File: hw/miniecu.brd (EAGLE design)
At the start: 50 x 50 mm, 59 parts

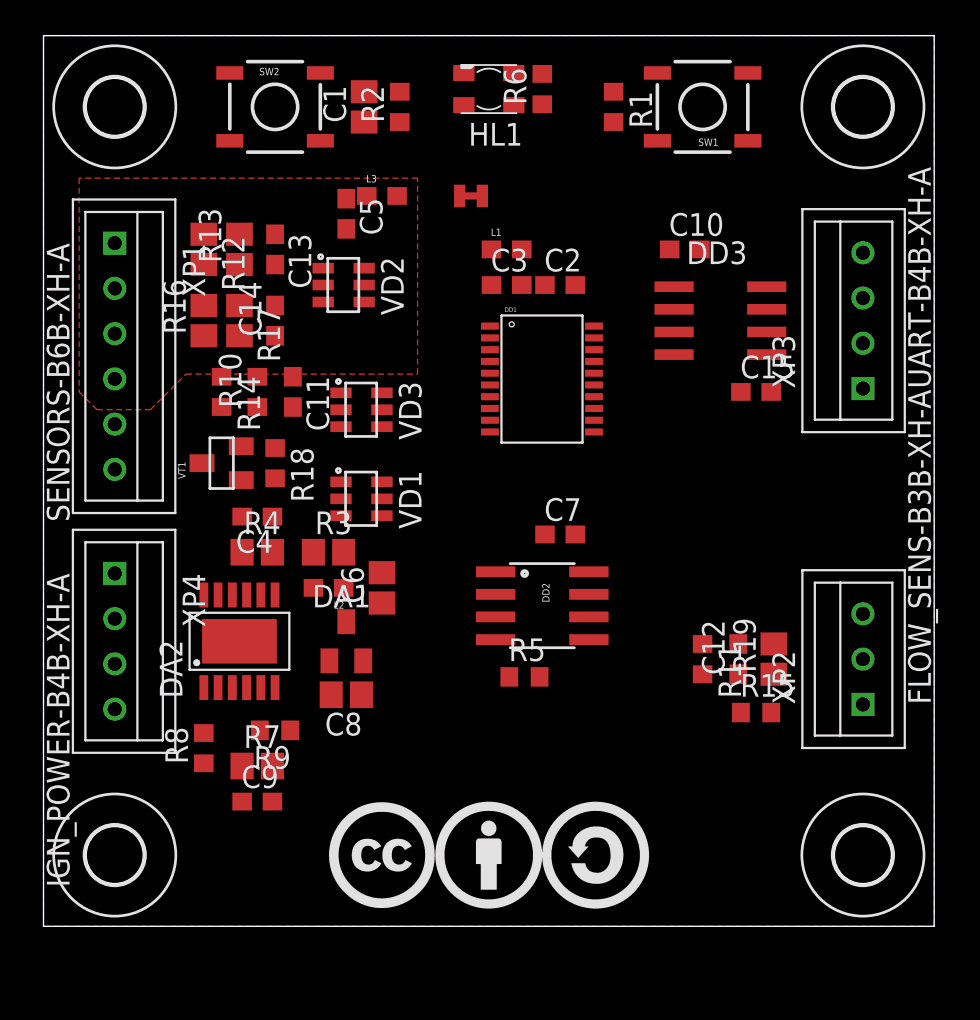
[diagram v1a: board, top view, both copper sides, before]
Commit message: use two resistors in voltage divider
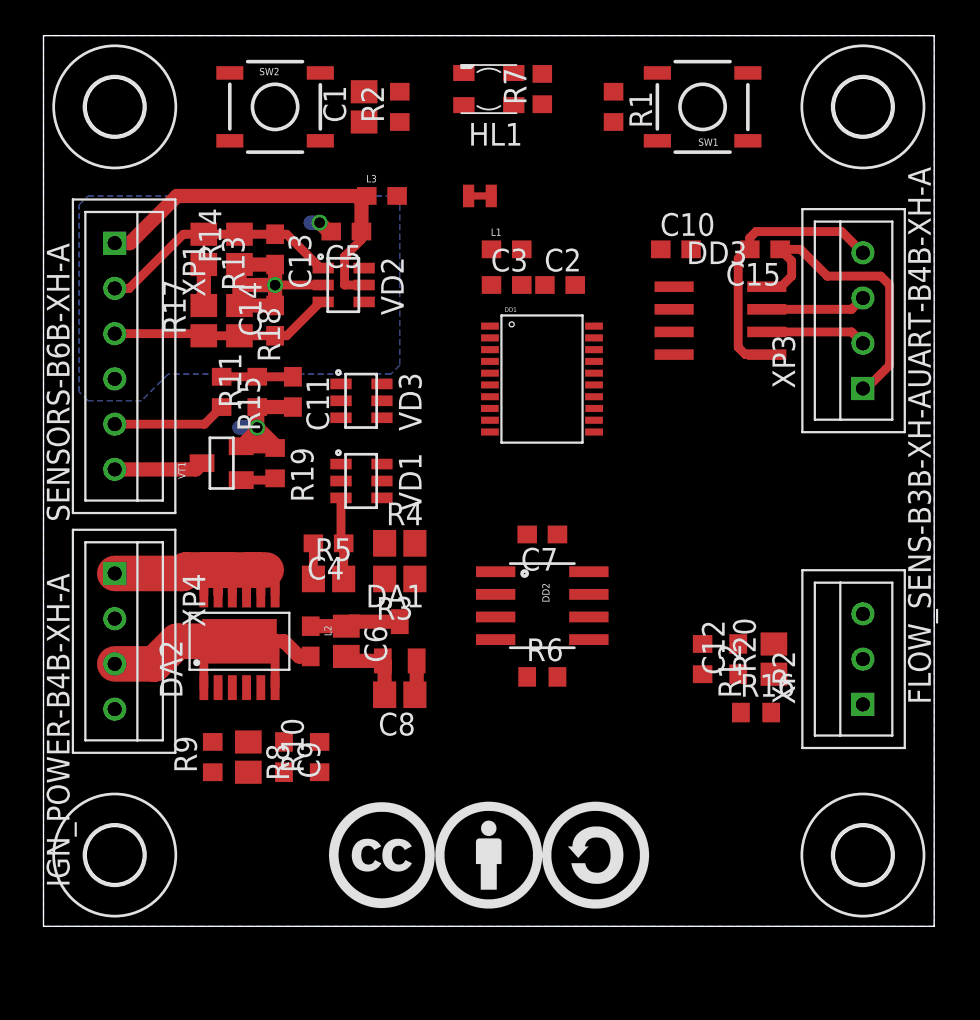
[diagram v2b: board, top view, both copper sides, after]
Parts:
- added R20: 10k, resistor:R0805
- R10, R13, R17: value np -> 10k
- R12: value 10k -> np; device resistor:R0805 -> resistor:R0603
- R14: value 100 -> np; device resistor:R0603 -> resistor:R0805
- R16: value 10k -> 100; device resistor:R0805 -> resistor:R0603
- R18: value 5.1k -> np; device resistor:R0603 -> resistor:R0805
- R19: value 10k -> 5.1k; device resistor:R0805 -> resistor:R0603
- R5: device resistor:R0603 -> resistor:R0805
- R6: value 140 -> 10k
- R7: value 10k -> 140; device resistor:R0805 -> resistor:R0603
- R8: value 100 -> 10k; device resistor:R0603 -> resistor:R0805
- R9: value 10k -> 100
- moved H1 42.0 mm to (46.0, 4.00)
- moved H2 42.0 mm to (4.00, 4.00)
- moved R7 41.2 mm to (28.0, 47.0), turned to 90 degrees
- moved R16 38.0 mm to (40.0, 12.0), turned to 0 degrees
- moved R12 36.2 mm to (37.0, 15.0)
- moved R15 35.0 mm to (10.0, 30.0), turned to 270 degrees
- moved R6 33.0 mm to (28.0, 14.0), turned to 0 degrees
- moved R19 30.1 mm to (13.0, 26.0), turned to 270 degrees
- moved R11 29.2 mm to (12.0, 30.0), turned to 90 degrees
- moved R10 20.8 mm to (15.5, 9.50)
- moved R5 12.3 mm to (16.0, 19.5)
- moved R18 8.25 mm to (11.0, 34.0)
- moved R14 8.06 mm to (11.0, 38.0), turned to 90 degrees
- moved C15 8.02 mm to (40.5, 38.0), turned to 180 degrees
- moved R4 8.02 mm to (20.0, 21.5)
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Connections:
- new net N$1: R3.1, R4.2
- net +3V3: now also R20.2, R6.2; no longer R19.2, R5.2
- net AGND: now also R14.1, R18.1; no longer R13.1, R17.1
- net AVCC_EXT: now also R13.2, R17.2; no longer R12.2, R16.2
- net FLOW_PULSE: now also R12.2, R16.1; no longer R11.2, R15.1
- net GND: now also R12.1, R19.1, R5.1, R8.2; no longer R18.1, R4.1, R7.2, R9.1
- net IGN_EN: now also R9.1; no longer R8.1
- net I_SENSE: now also R8.1; no longer R7.1
- net LED: now also R7.1; no longer R6.1
- net N$2: now also R7.2; no longer R6.2
- net N$3: now also R6.1; no longer R5.1
- net N$4: now also R16.2, R20.1; no longer R15.2, R19.1
- net N$7: now also R9.2; no longer R8.2
- net N$9: now also R10.2; no longer R9.2
- net OIL_PRES: now also R17.1, R18.2; no longer R16.1, R17.2
- net RPM_IN: now also R11.2, R15.1; no longer R10.2, R14.1
- net RPM_IN_CON: now also R15.2; no longer R14.2
- net STARTER: now also R19.2; no longer R18.2
- net THERM: now also R13.1, R14.2; no longer R12.1, R13.2
- net V_SENSE: now also R4.1, R5.2; no longer R3.1, R4.2
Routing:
- net AVCC_EXT: track 0.00 -> 24.2 mm
- net V_IGN: track 0.00 -> 19.0 mm
- net VBAT: track 0.00 -> 17.1 mm
- net VCC2: track 0.00 -> 16.9 mm
- net AGND: track 0.00 -> 15.5 mm, vias 0 -> 2
- net GND: track 0.00 -> 15.4 mm, vias 0 -> 1
- net GND2: track 0.00 -> 15.3 mm
- net THERM: track 0.00 -> 13.7 mm
- net OIL_PRES: track 0.00 -> 12.5 mm
- net RPM_IN_CON: track 0.00 -> 6.40 mm
- net IOTXD: track 0.00 -> 5.66 mm
- net IORXD: track 0.00 -> 5.66 mm
- net N$6: track 0.00 -> 5.10 mm
- net STARTER_OUT: track 0.00 -> 5.04 mm
- net V_SENSE: track 0.00 -> 4.61 mm
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- added copper zone on layer 16, net AGND
- removed copper zone on layer 1, net AGND

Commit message: pcb: routing done
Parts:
- removed R20: 10k, resistor:R0805
- removed U$1: CREATIVE_COMMONS_BY-SA, logo:CC-BY-SA-6MM
- added LOGO1: OSHW-LOGOL, SparkFun-Aesthetics:OSHW-LOGO-L
- R10, R13, R17: value 10k -> np
- R12: value np -> 10k; device resistor:R0603 -> resistor:R0805
- R14: value np -> 100; device resistor:R0805 -> resistor:R0603
- R16: value 100 -> 10k; device resistor:R0603 -> resistor:R0805
- R18: value np -> 5.1k; device resistor:R0805 -> resistor:R0603
- R19: value 5.1k -> 10k; device resistor:R0603 -> resistor:R0805
- R6: value 10k -> 140
- R7: value 140 -> 10k; device resistor:R0603 -> resistor:R0805
- R8: value 10k -> 100; device resistor:R0805 -> resistor:R0603
- R9: value 100 -> 10k
- moved R7 41.0 mm to (11.5, 9.50), turned to 270 degrees
- moved R16 38.0 mm to (9.00, 34.0), turned to 90 degrees
- moved R12 36.2 mm to (9.00, 38.0)
- moved R15 35.0 mm to (40.0, 12.0), turned to 0 degrees
- moved R6 33.0 mm to (28.0, 47.0), turned to 90 degrees
- moved R19 30.1 mm to (41.0, 15.0), turned to 90 degrees
- moved R11 29.2 mm to (37.0, 15.0), turned to 270 degrees
- moved R10 20.8 mm to (12.0, 30.0)
- moved PT1 10.2 mm to (26.5, 31.0), flipped to the bottom
- moved R18 8.25 mm to (13.0, 26.0)
- moved R14 8.06 mm to (10.0, 30.0), turned to 270 degrees
- moved R9 6.00 mm to (15.5, 9.50)
- moved C7 3.64 mm to (24.5, 21.0), turned to 270 degrees
- moved DD2 3.00 mm to (28.0, 21.0), turned to 0 degrees
- moved R13 2.00 mm to (11.0, 38.0), turned to 90 degrees
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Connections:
- removed net N$3: DD2.3, R6.1
- net +3V3: now also DD2.3, R19.2; no longer R20.2, R6.2
- net AGND: now also R13.1, R17.1; no longer R14.1, R18.1
- net AVCC_EXT: now also R12.2, R16.2; no longer R13.2, R17.2
- net FLASH_CS: now also DD1.19; no longer DD1.3
- net FLOW_PULSE: now also R11.2, R15.1; no longer R12.2, R16.1
- net GND: now also R18.1, R7.2, R9.1; no longer R12.1, R19.1, R8.2
- net IGN_EN: now also R8.1; no longer R9.1
- net I_SENSE: now also R7.1; no longer R8.1
- net LED: now also R6.1; no longer R7.1
- net N$2: now also R6.2; no longer R7.2
- net N$4: now also R15.2, R19.1; no longer R16.2, R20.1
- net N$7: now also R8.2; no longer R9.2
- net N$9: now also R9.2; no longer R10.2
- net OIL_PRES: now also R16.1, R17.2; no longer R17.1, R18.2
- net RPM_IN: now also R10.2, R14.1; no longer R11.2, R15.1
- net RPM_IN_CON: now also R14.2; no longer R15.2
- net STARTER: now also DD1.3, R18.2; no longer DD1.19, R19.2
- net THERM: now also R12.1, R13.2; no longer R13.1, R14.2
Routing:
- net +3V3: track 1.94 -> 151.8 mm, vias 0 -> 10
- net GND: track 15.4 -> 92.6 mm, vias 1 -> 12
- net FLOW_PULSE: track 0.00 -> 52.7 mm, vias 0 -> 4
- net IGN_EN: track 0.00 -> 45.6 mm, vias 0 -> 2
- net I_SENSE: track 0.00 -> 34.1 mm, vias 0 -> 2
- net !NRST: track 0.00 -> 26.8 mm
- net BOOT0: track 0.00 -> 25.7 mm
- net FLASH_CS: track 0.00 -> 20.7 mm, vias 0 -> 2
- net STARTER: track 1.94 -> 18.5 mm, vias 0 -> 2
- net LED: track 0.00 -> 16.3 mm
- net OIL_PRES: track 12.5 -> 25.7 mm, vias 0 -> 2
- net MISO: track 0.00 -> 12.4 mm
- net AVCC_EXT: track 24.2 -> 36.1 mm
- net THERM: track 13.7 -> 25.0 mm
- net V_SENSE: track 4.61 -> 14.8 mm
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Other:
- board text added: "RAP-UAV"
